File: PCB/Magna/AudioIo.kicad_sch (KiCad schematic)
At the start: 15 parts, among them U201 24.576 MHz, U202 CY2305SXC-1HT, U203 CY2305SXC-1HT

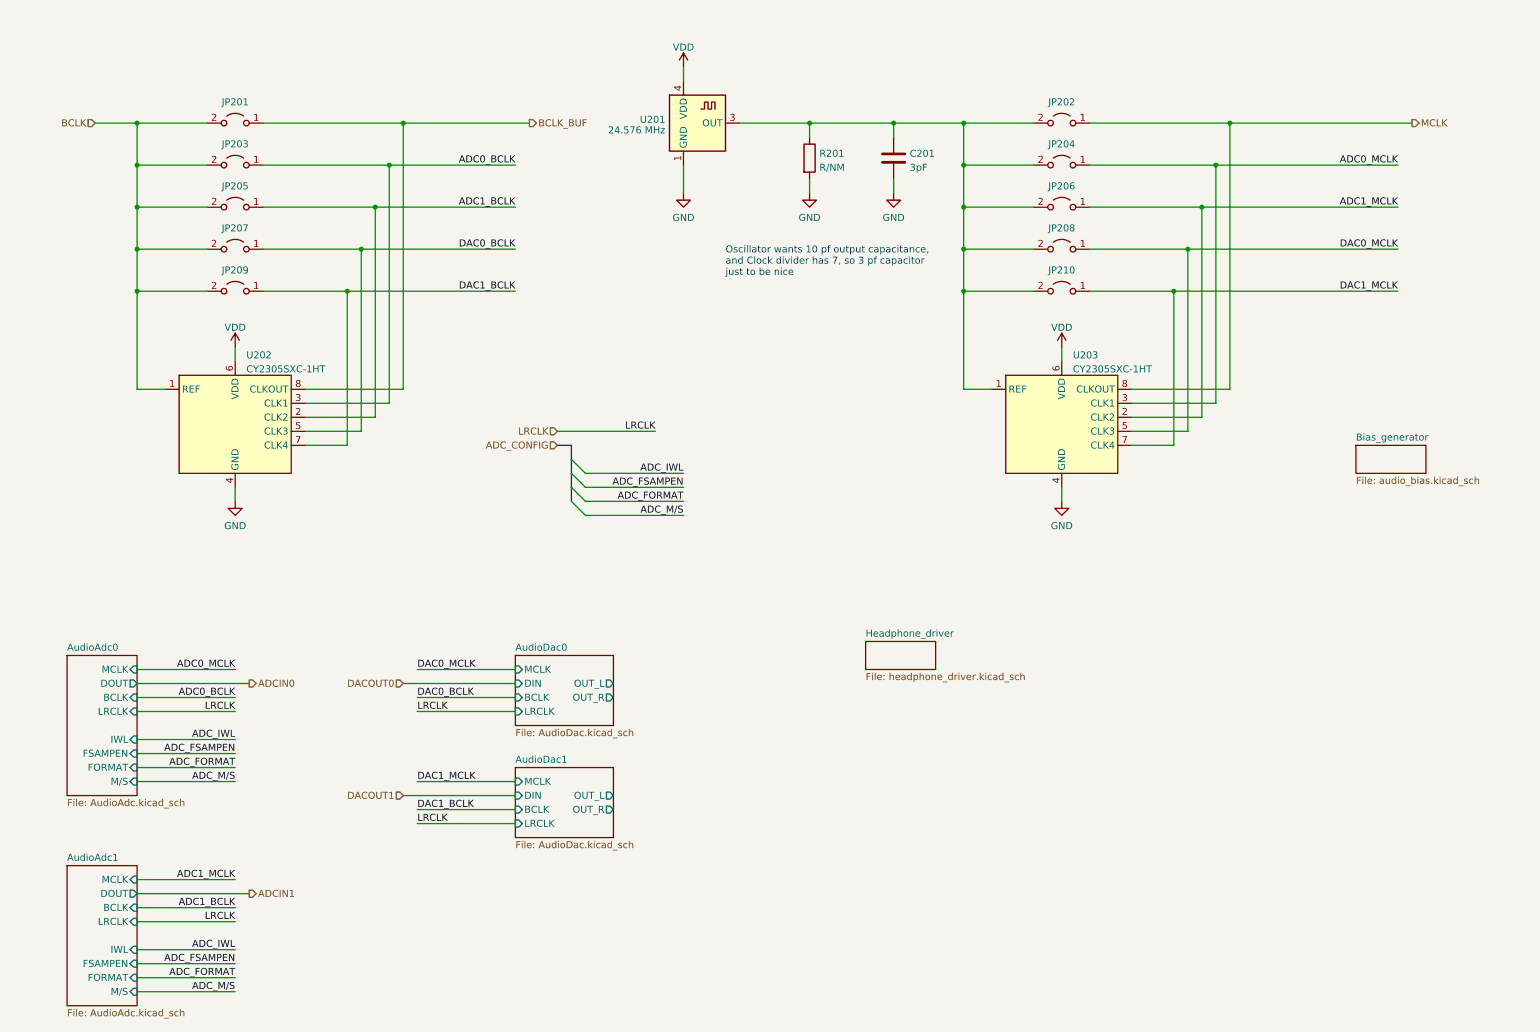
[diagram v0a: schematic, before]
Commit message: Update analogue frontend and add potentiometer interface
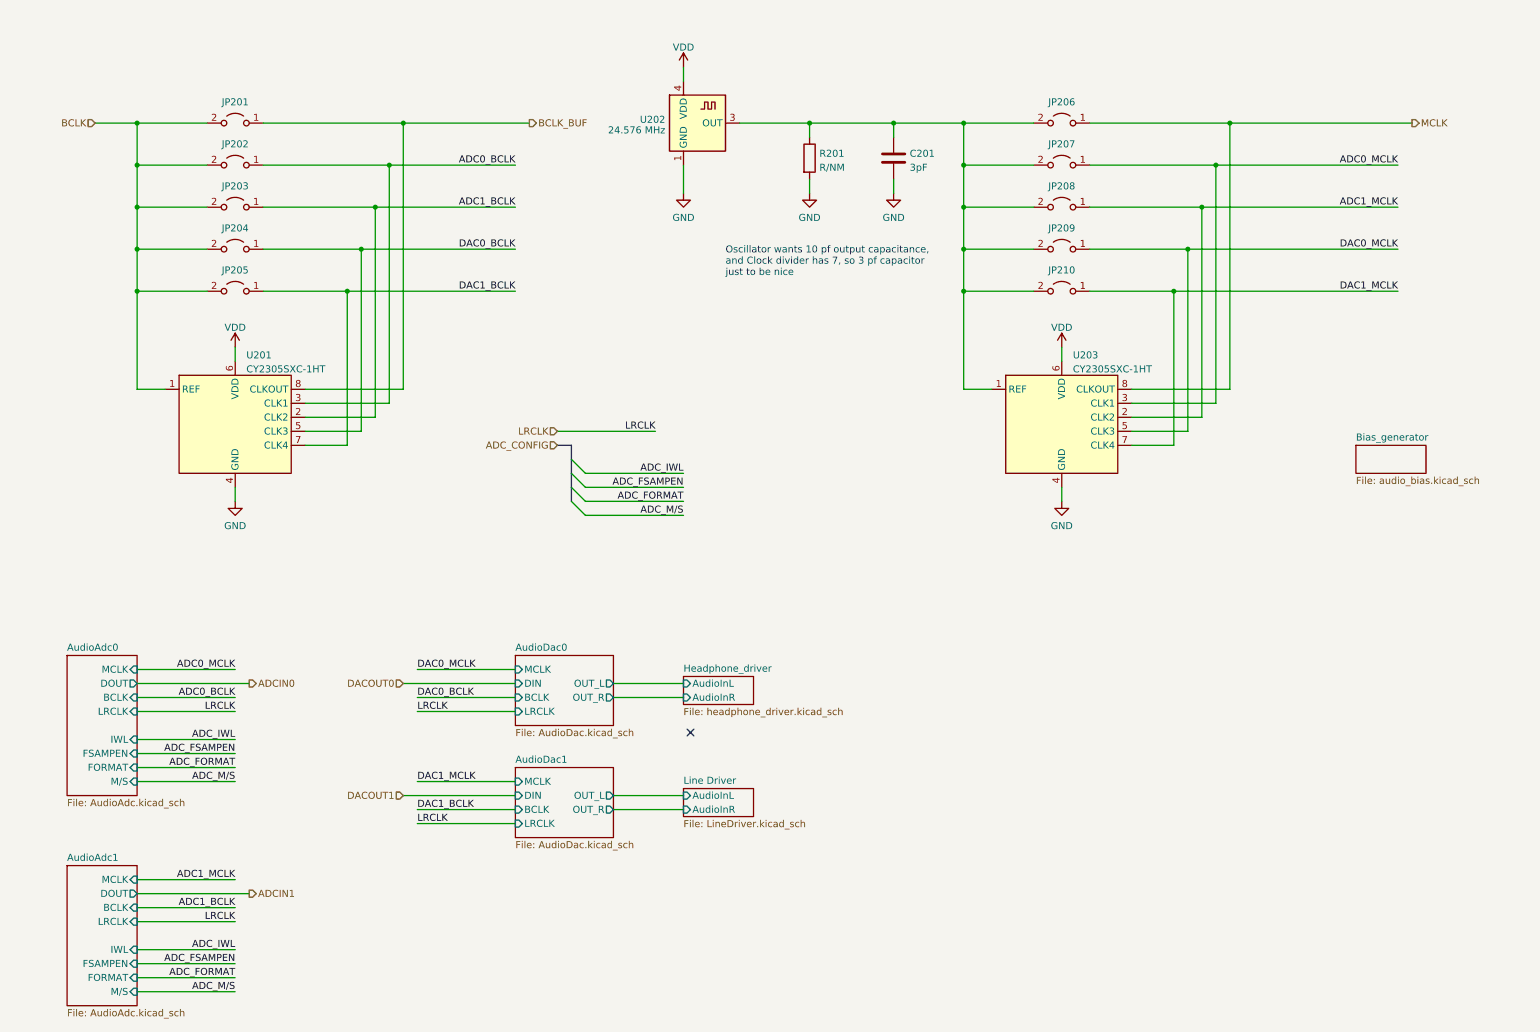
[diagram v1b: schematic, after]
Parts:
- renumbered JP203 to JP202, JP205 to JP203, JP207 to JP204, JP209 to JP205, JP202 to JP206, JP204 to JP207, JP206 to JP208, JP208 to JP209, U202 to U201, U201 to U202
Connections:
- no-connect marks 0 -> 1
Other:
- added sheet Line Driver (LineDriver.kicad_sch)
- sheet Headphone_driver ports: added AudioInL, AudioInR; removed none

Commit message: Add final touched to all schematics
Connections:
- net BCLK_BUF: no longer names the net of JP201.1 (A), U201.8 (CLKOUT)
- no-connect marks 1 -> 0
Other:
- note added: "ADC and DAC blocks"
- note added: "BCLK distribution"
- note added: "Bias Generator"
- note added: "Input signal breakout"
- note added: "MCLK Generation and distribution"
- moved on the sheet: C201, JP201, JP202, JP203, JP204, JP205, JP206, JP207, JP208, JP209, JP210, R201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

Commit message: Remove all ERC in schematics
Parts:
- U203: LCSC (none) -> CY2305
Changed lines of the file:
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@@
     (effects (font (size 1.27 1.27)) (justify right bottom))
   )
-  (label "ADC_FSAMPEN" (at 274.32 147.32 180)
+  (label "ADC_FSAMPEN" (at 274.32 147.32 180) (fields_autoplaced)
     (effects (font (size 1.27 1.27)) (justify right bottom))
   )
@@
     (effects (font (size 1.27 1.27)) (justify right bottom))
   )
-  (label "ADC_IWL" (at 274.32 144.78 180)
+  (label "ADC_IWL" (at 274.32 144.78 180) (fields_autoplaced)
     (effects (font (size 1.27 1.27)) (justify right bottom))
   )
@@
     (effects (font (size 1.27 1.27)) (justify right bottom))
   )
-  (label "ADC_M{slash}S" (at 274.32 152.4 180)
+  (label "ADC_M{slash}S" (at 274.32 152.4 180) (fields_autoplaced)
     (effects (font (size 1.27 1.27)) (justify right bottom))
   )
@@
     (effects (font (size 1.27 1.27)) (justify left bottom))
   )
-  (label "ADC_FORMAT" (at 274.32 149.86 180)
+  (label "ADC_FORMAT" (at 274.32 149.86 180) (fields_autoplaced)
     (effects (font (size 1.27 1.27)) (justify right bottom))
   )
@@
       (effects (font (size 1.27 1.27)) hide)
     )
-    (property "Datasheet" "" (at 99.06 86.36 0)
-      (effects (font (size 1.27 1.27)) hide)
-    )
+    (property "Datasheet" "https://datasheet.lcsc.com/lcsc/2011101039_Cypress-Semicon-CY2305SXC-1HT_C914887.pdf" (at 99.06 86.36 0)
+      (effects (font (size 1.27 1.27)) hide)
+    )
+    (property "LCSC" "CY2305" (at 99.06 86.36 0)
+      (effects (font (size 1.27 1.27)) hide)
+    )

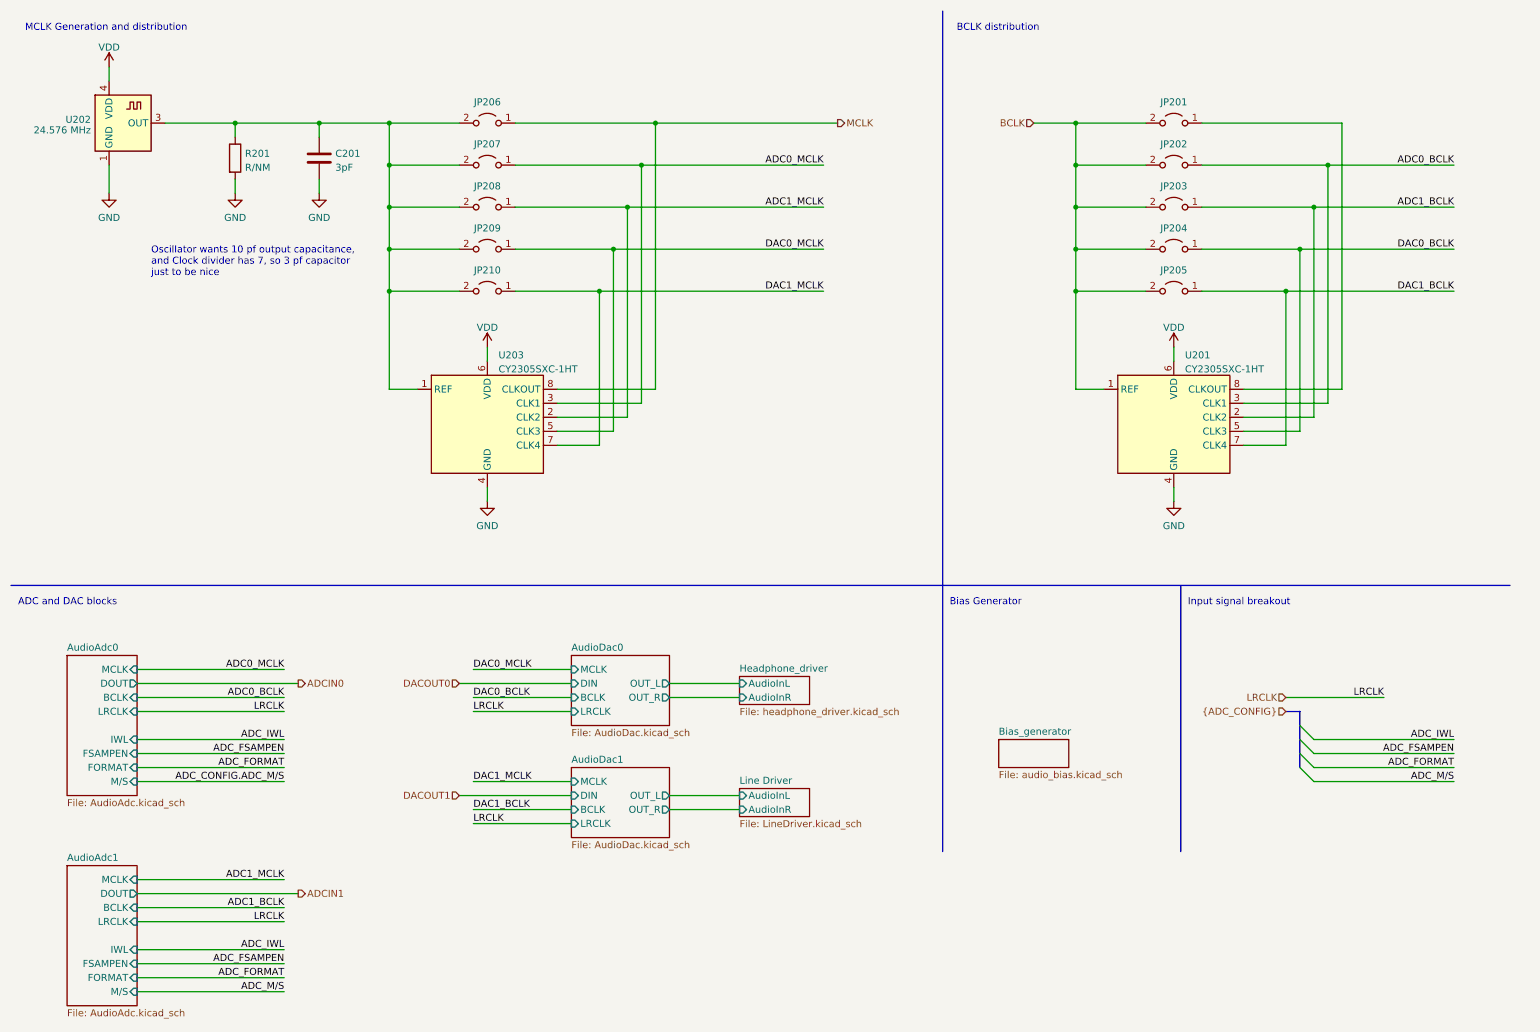
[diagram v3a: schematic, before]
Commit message: Update capacitors to parts in JLC library
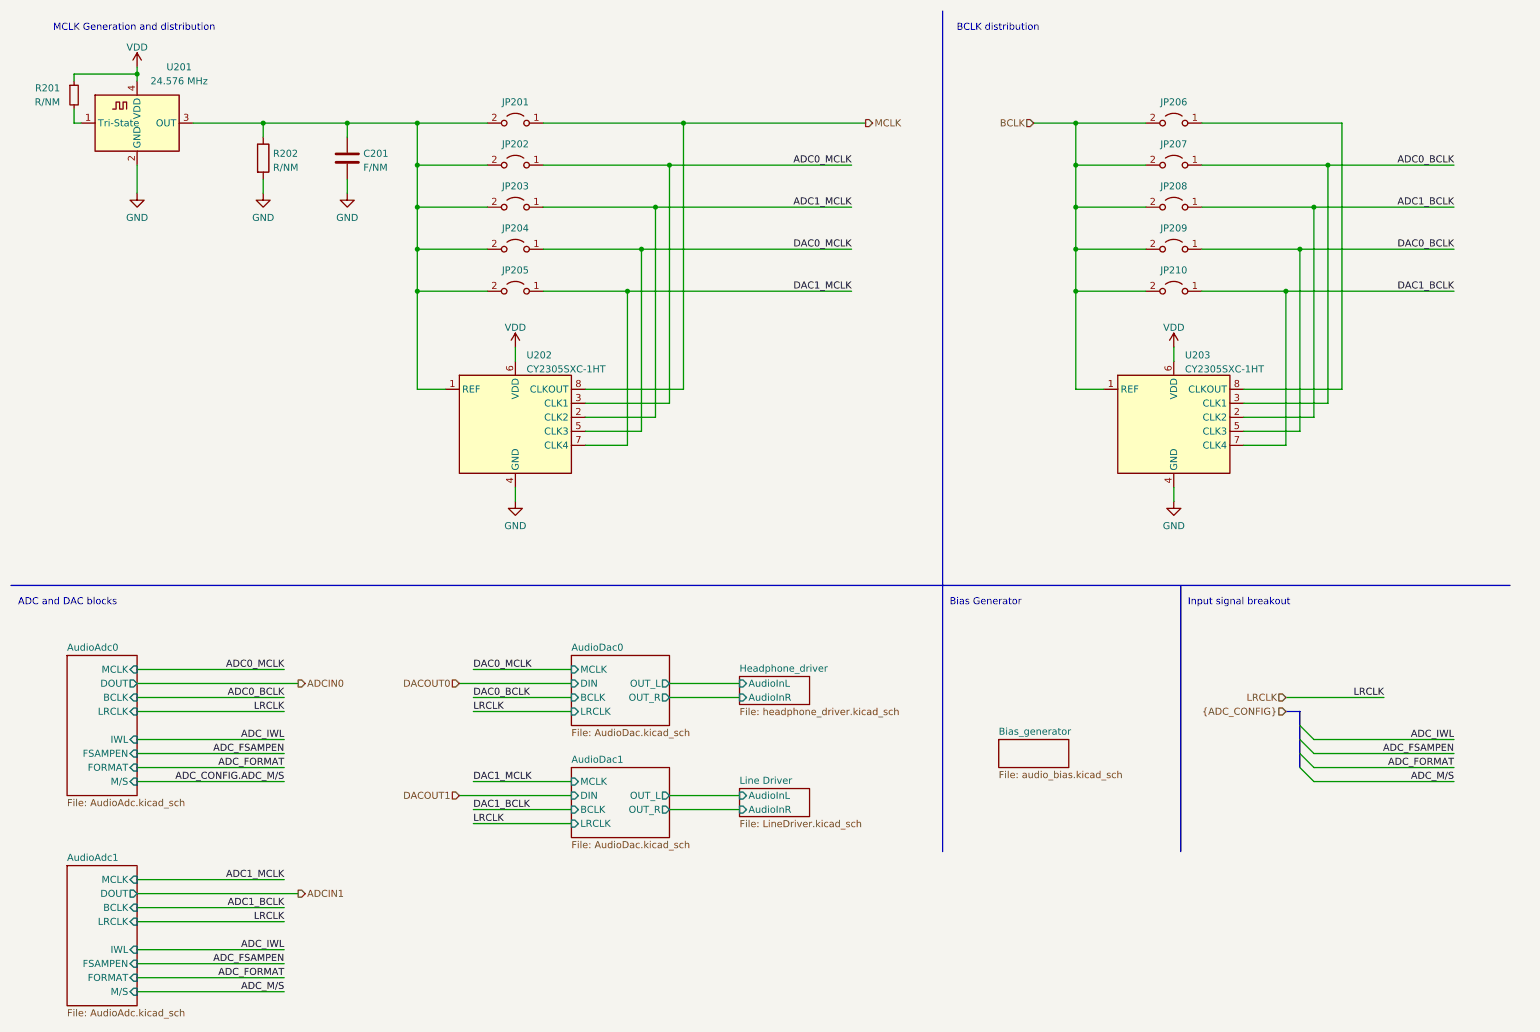
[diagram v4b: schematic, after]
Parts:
- added R201: R/NM, symbol Device:R_Small
- C201: value 3pF -> F/NM; LCSC C46219 -> (none)
- U201: renamed from U202; footprint Oscillator:Oscillator_SMD_Abracon_ASE-4Pin_3.2x2.5mm -> Oscillator:Oscillator_SMD_Abracon_ASE-4Pin_3.2x2.5mm_HandSoldering; symbol Oscillator:FT5HN -> Oscillator:ECS-2520MV-xxx-xx
- renumbered JP206 to JP201, JP207 to JP202, JP208 to JP203, JP209 to JP204, JP210 to JP205, JP201 to JP206, JP202 to JP207, JP203 to JP208, JP204 to JP209, JP205 to JP210, R201 to R202, U203 to U202, U201 to U203
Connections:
- net GND: no longer U201.1 (GND)
- net VDD: now also R201.1
- new net: R201.2, U201.1 (Tri-State)
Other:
- note removed: "Oscillator wants 10 pf output capacitance, and Clock divider has 7, so 3 pf capacitor just to be nice"
- moved on the sheet: C201, JP201, JP202, JP203, JP204, JP205, R202, U202

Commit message: Select parts for all components
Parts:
- JP201, JP202, JP203, JP204, JP205, JP206, JP207, JP208, JP209, JP210: footprint (none) -> Jumper:SolderJumper-2_P1.3mm_Open_TrianglePad1.0x1.5mm
- R201, R202: footprint (none) -> Resistor_SMD:R_0805_2012Metric
- U202, U203: LCSC CY2305 -> C914887
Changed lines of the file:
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@@
       (effects (font (size 1.27 1.27)) hide)
     )
-    (property "LCSC" "CY2305" (at 223.52 86.36 0)
+    (property "LCSC" "C914887" (at 223.52 86.36 0)
       (effects (font (size 1.27 1.27)) hide)
     )
@@
       (effects (font (size 1.27 1.27)) hide)
     )
-    (property "Footprint" "" (at 104.14 55.88 0)
+    (property "Footprint" "Jumper:SolderJumper-2_P1.3mm_Open_TrianglePad1.0x1.5mm" (at 104.14 55.88 0)
       (effects (font (size 1.27 1.27)) hide)
     )
@@
       (effects (font (size 1.27 1.27)) hide)
     )
-    (property "Footprint" "" (at 104.14 48.26 0)
+    (property "Footprint" "Jumper:SolderJumper-2_P1.3mm_Open_TrianglePad1.0x1.5mm" (at 104.14 48.26 0)
       (effects (font (size 1.27 1.27)) hide)
     )
@@
       (effects (font (size 1.27 1.27)) hide)
     )
-    (property "Footprint" "" (at 223.52 63.5 0)
+    (property "Footprint" "Jumper:SolderJumper-2_P1.3mm_Open_TrianglePad1.0x1.5mm" (at 223.52 63.5 0)
       (effects (font (size 1.27 1.27)) hide)
     )
@@
       (effects (font (size 1.27 1.27)) (justify right))
     )
-    (property "Footprint" "" (at 24.13 27.94 0)
+    (property "Footprint" "Resistor_SMD:R_0805_2012Metric" (at 24.13 27.94 0)
       (effects (font (size 1.27 1.27)) hide)
     )
@@
       (effects (font (size 1.27 1.27)) hide)
     )
-    (property "Footprint" "" (at 223.52 55.88 0)
+    (property "Footprint" "Jumper:SolderJumper-2_P1.3mm_Open_TrianglePad1.0x1.5mm" (at 223.52 55.88 0)
       (effects (font (size 1.27 1.27)) hide)
     )
@@
       (effects (font (size 1.27 1.27)) hide)
     )
-    (property "Footprint" "" (at 223.52 40.64 0)
+    (property "Footprint" "Jumper:SolderJumper-2_P1.3mm_Open_TrianglePad1.0x1.5mm" (at 223.52 40.64 0)
       (effects (font (size 1.27 1.27)) hide)
     )
@@
       (effects (font (size 1.27 1.27)) hide)
     )
-    (property "Footprint" "" (at 223.52 33.02 0)
+    (property "Footprint" "Jumper:SolderJumper-2_P1.3mm_Open_TrianglePad1.0x1.5mm" (at 223.52 33.02 0)
       (effects (font (size 1.27 1.27)) hide)
     )
@@
       (effects (font (size 1.27 1.27)) hide)
     )
-    (property "Footprint" "" (at 104.14 33.02 0)
+    (property "Footprint" "Jumper:SolderJumper-2_P1.3mm_Open_TrianglePad1.0x1.5mm" (at 104.14 33.02 0)
       (effects (font (size 1.27 1.27)) hide)
     )
@@
       (effects (font (size 1.27 1.27)) (justify left))
     )
-    (property "Footprint" "" (at 56.642 39.37 90)
+    (property "Footprint" "Resistor_SMD:R_0805_2012Metric" (at 56.642 39.37 90)
       (effects (font (size 1.27 1.27)) hide)
     )
@@
       (effects (font (size 1.27 1.27)) hide)
     )
-    (property "Footprint" "" (at 104.14 40.64 0)
+    (property "Footprint" "Jumper:SolderJumper-2_P1.3mm_Open_TrianglePad1.0x1.5mm" (at 104.14 40.64 0)
       (effects (font (size 1.27 1.27)) hide)
     )
@@
       (effects (font (size 1.27 1.27)) hide)
     )
-    (property "Footprint" "" (at 104.14 63.5 0)
+    (property "Footprint" "Jumper:SolderJumper-2_P1.3mm_Open_TrianglePad1.0x1.5mm" (at 104.14 63.5 0)
       (effects (font (size 1.27 1.27)) hide)
     )
@@
       (effects (font (size 1.27 1.27)) hide)
     )
-    (property "Footprint" "" (at 223.52 48.26 0)
+    (property "Footprint" "Jumper:SolderJumper-2_P1.3mm_Open_TrianglePad1.0x1.5mm" (at 223.52 48.26 0)
       (effects (font (size 1.27 1.27)) hide)
     )
@@
       (effects (font (size 1.27 1.27)) hide)
     )
-    (property "LCSC" "CY2305" (at 104.14 86.36 0)
-      (effects (font (size 1.27 1.27)) hide)
-    )
+    (property "LCSC" "C914887" (at 104.14 86.36 0)
+      (effects (font (size 1.27 1.27)) hide)
+    )

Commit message: Add even more component footprints and partnumbers
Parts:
- C201: footprint Capacitor_SMD:C_0603_1608Metric -> Capacitor_SMD:C_0603_1608Metric_Pad1.08x0.95mm_HandSolder
- R201, R202: footprint Resistor_SMD:R_0805_2012Metric -> Resistor_SMD:R_0805_2012Metric_Pad1.20x1.40mm_HandSolder
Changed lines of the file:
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@@
       (effects (font (size 1.27 1.27)) (justify right))
     )
-    (property "Footprint" "Resistor_SMD:R_0805_2012Metric" (at 24.13 27.94 0)
+    (property "Footprint" "Resistor_SMD:R_0805_2012Metric_Pad1.20x1.40mm_HandSolder" (at 24.13 27.94 0)
       (effects (font (size 1.27 1.27)) hide)
     )
@@
       (effects (font (size 1.27 1.27)) (justify left))
     )
-    (property "Footprint" "Resistor_SMD:R_0805_2012Metric" (at 56.642 39.37 90)
+    (property "Footprint" "Resistor_SMD:R_0805_2012Metric_Pad1.20x1.40mm_HandSolder" (at 56.642 39.37 90)
       (effects (font (size 1.27 1.27)) hide)
     )
@@
       (effects (font (size 1.27 1.27)) (justify left))
     )
-    (property "Footprint" "Capacitor_SMD:C_0603_1608Metric" (at 74.6252 43.18 0)
-      (effects (font (size 1.27 1.27)) hide)
-    )
+    (property "Footprint" "Capacitor_SMD:C_0603_1608Metric_Pad1.08x0.95mm_HandSolder" (at 74.6252 43.18 0)
+      (effects (font (size 1.27 1.27)) hide)
+    )
